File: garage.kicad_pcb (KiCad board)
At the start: 2 copper layers, 61 x 71.1 mm, 9 parts, among them P1 CONN_02X25, P2 CONN_01X02, P3 CONN_02X25, P4 CONN_01X20, P5 CONN_01X20, Q1 2N3904

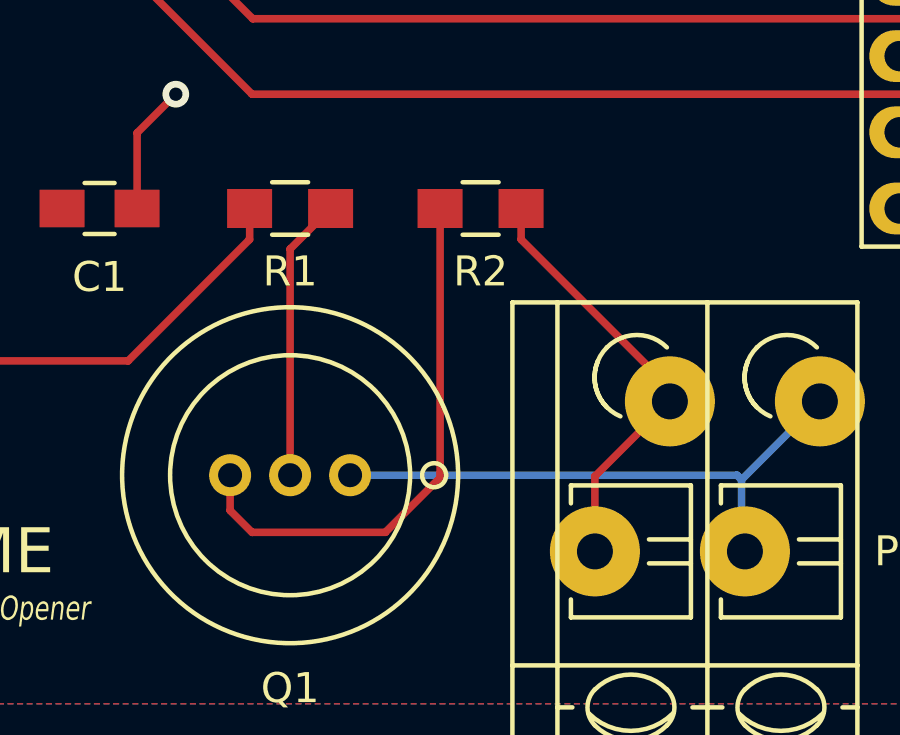
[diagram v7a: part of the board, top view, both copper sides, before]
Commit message: Removed R2
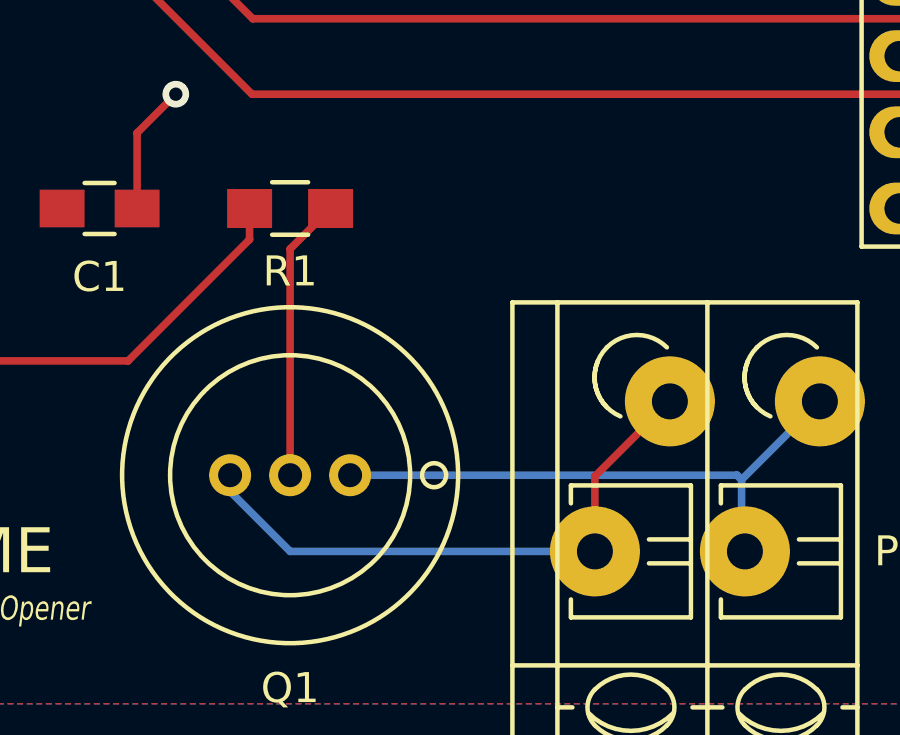
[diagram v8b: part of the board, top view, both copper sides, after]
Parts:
- removed R2: 220, Resistors_SMD:R_0805_HandSoldering
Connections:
- Q1 pad 3: Net-(Q1-Pad3) -> Garage+
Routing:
- net Net-(Q1-Pad3): track 18.2 -> 0.00 mm
- net Garage+: track 14.5 -> 20.0 mm
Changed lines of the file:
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@@
 (kicad_pcb (version 4) (host pcbnew "(2015-01-16 BZR 5376)-product")
   (general
-    (links 20)
+    (links 19)
     (no_connects 0)
     (area 54.559999 31.699999 120.022334 103.899)
     (thickness 1.6)
     (drawings 7)
-    (tracks 73)
+    (tracks 69)
     (zones 0)
-    (modules 9)
-    (nets 134)
+    (modules 8)
+    (nets 133)
   )
   (page A4)
@@
   (net 131 "Net-(P5-Pad19)")
   (net 132 "Net-(Q1-Pad2)")
-  (net 133 "Net-(Q1-Pad3)")
   (net_class Default "This is the default net class."
     (clearance 0.254)
@@
     (add_net "Net-(P5-Pad9)")
     (add_net "Net-(Q1-Pad2)")
-    (add_net "Net-(Q1-Pad3)")
     (add_net PA1)
     (add_net PA8)
@@
       (net 2 GND))
     (pad 3 thru_hole circle (at 2 0 180) (size 1.4 1.4) (drill 0.8) (layers *.Cu *.Mask F.SilkS)
-      (net 133 "Net-(Q1-Pad3)"))
+      (net 53 Garage+))
     (model Transistors_OldSowjetAera.3dshapes/OldSowjetaera_Transistor_Type-I_SmallPads.wrl
       (at (xyz 0 0 0))
@@
     (pad 2 smd rect (at 1.35 0 180) (size 1.5 1.3) (layers F.Cu F.Paste F.Mask)
       (net 94 PA8))
-    (model Resistors_SMD.3dshapes/R_0805_HandSoldering.wrl
-      (at (xyz 0 0 0))
-      (scale (xyz 1 1 1))
-      (rotate (xyz 0 0 0))
-    )
-  )
-  (module Resistors_SMD:R_0805_HandSoldering (layer F.Cu)
-    (at 87.63 85.09 180)
-    (descr "Resistor SMD 0805, hand soldering")
-    (tags "resistor 0805")
-    (attr smd)
-    (fp_text reference R2 (at 0 -2.1 180) (layer F.SilkS)
-      (effects (font (size 1 1) (thickness 0.15)))
-    )
-    (fp_text value 220 (at 0 2.1 180) (layer F.Fab) hide
-      (effects (font (size 1 1) (thickness 0.15)))
-    )
-    (fp_line (start -2.4 -1) (end 2.4 -1) (layer F.CrtYd) (width 0.05))
-    (fp_line (start -2.4 1) (end 2.4 1) (layer F.CrtYd) (width 0.05))
-    (fp_line (start -2.4 -1) (end -2.4 1) (layer F.CrtYd) (width 0.05))
-    (fp_line (start 2.4 -1) (end 2.4 1) (layer F.CrtYd) (width 0.05))
-    (fp_line (start 0.6 0.875) (end -0.6 0.875) (layer F.SilkS) (width 0.15))
-    (fp_line (start -0.6 -0.875) (end 0.6 -0.875) (layer F.SilkS) (width 0.15))
-    (pad 1 smd rect (at -1.35 0 180) (size 1.5 1.3) (layers F.Cu F.Paste F.Mask)
-      (net 53 Garage+))
-    (pad 2 smd rect (at 1.35 0 180) (size 1.5 1.3) (layers F.Cu F.Paste F.Mask)
-      (net 133 "Net-(Q1-Pad3)"))
     (model Resistors_SMD.3dshapes/R_0805_HandSoldering.wrl
       (at (xyz 0 0 0))
@@
   (segment (start 93.9394 91.5187) (end 91.44 94.0181) (width 0.254) (layer F.Cu) (net 53) (status 10))
   (segment (start 91.44 94.0181) (end 91.44 96.52) (width 0.254) (layer F.Cu) (net 53) (status 20))
-  (segment (start 88.98 86.1213) (end 93.9394 91.0807) (width 0.254) (layer F.Cu) (net 53) (status 20))
   (segment (start 93.9394 91.0807) (end 93.9394 91.5187) (width 0.254) (layer F.Cu) (net 53) (status 30))
-  (segment (start 88.98 85.09) (end 88.98 86.1213) (width 0.254) (layer F.Cu) (net 53) (status 10))
+  (segment (start 81.28 96.52) (end 91.44 96.52) (width 0.254) (layer B.Cu) (net 53))
+  (segment (start 79.28 94.52) (end 81.28 96.52) (width 0.254) (layer B.Cu) (net 53))
+  (segment (start 79.28 93.98) (end 79.28 94.52) (width 0.254) (layer B.Cu) (net 53))
   (segment (start 79.93 85.09) (end 79.93 86.1213) (width 0.254) (layer F.Cu) (net 94) (status 10))
   (segment (start 79.93 86.1213) (end 75.8813 90.17) (width 0.254) (layer F.Cu) (net 94))
@@
   (segment (start 81.28 93.98) (end 81.28 86.44) (width 0.254) (layer F.Cu) (net 132))
   (segment (start 81.28 86.44) (end 82.63 85.09) (width 0.254) (layer F.Cu) (net 132))
-  (segment (start 79.28 93.98) (end 79.28 95.155) (width 0.254) (layer F.Cu) (net 133))
-  (segment (start 86.28 94.06) (end 86.28 85.09) (width 0.254) (layer F.Cu) (net 133))
-  (segment (start 84.455 95.885) (end 86.28 94.06) (width 0.254) (layer F.Cu) (net 133))
-  (segment (start 80.01 95.885) (end 84.455 95.885) (width 0.254) (layer F.Cu) (net 133))
-  (segment (start 79.28 95.155) (end 80.01 95.885) (width 0.254) (layer F.Cu) (net 133))
   (zone (net 1) (net_name 3V) (layer F.Cu) (hatch edge 0.508)
     (connect_pads (clearance 0.508))
